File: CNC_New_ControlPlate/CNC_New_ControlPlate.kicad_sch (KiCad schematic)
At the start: 5 parts, among them J1 OTHER, J2 Conn_01x02, J3 STEPPERS, J4 SPINDEL

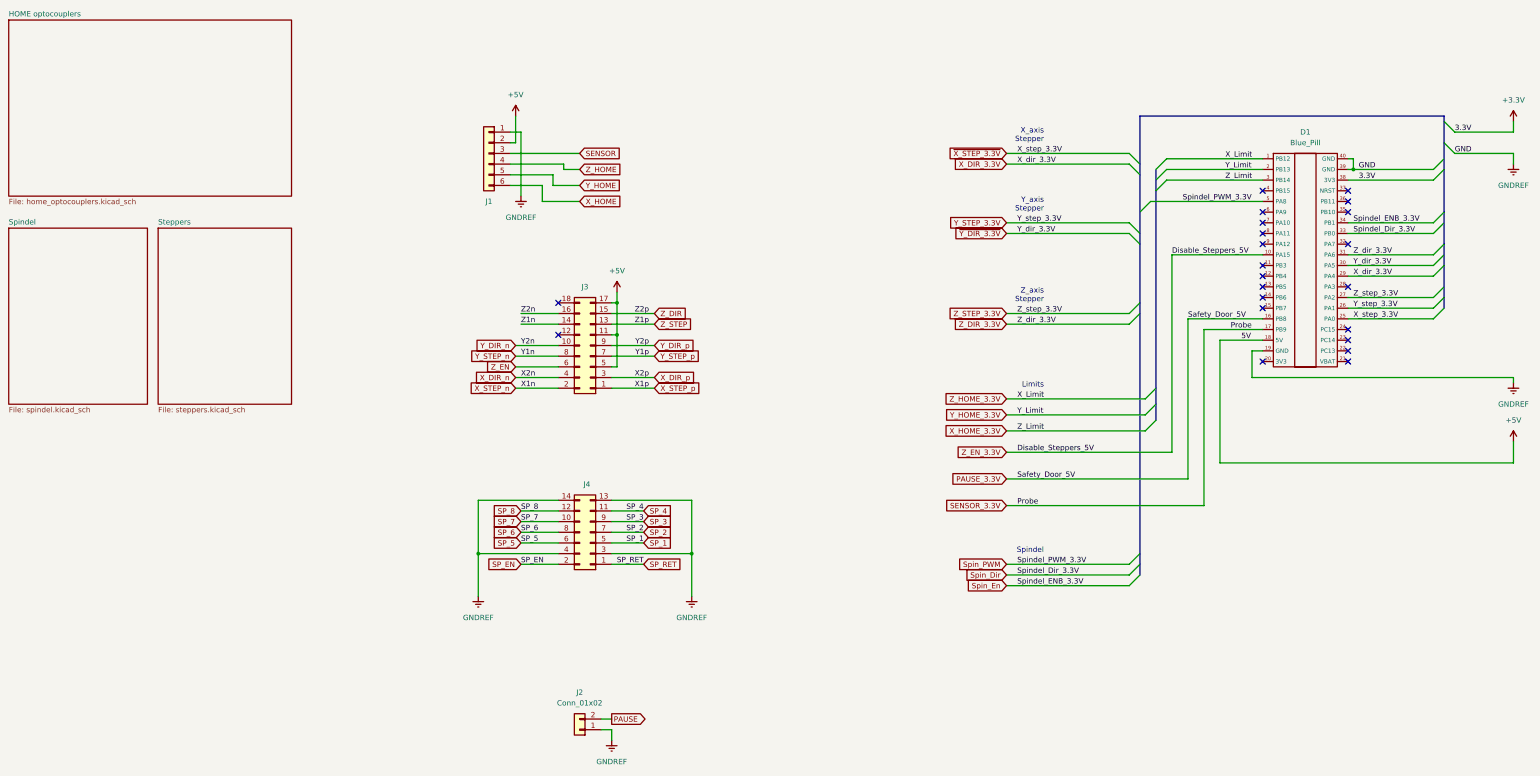
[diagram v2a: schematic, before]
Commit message: Edit footprints
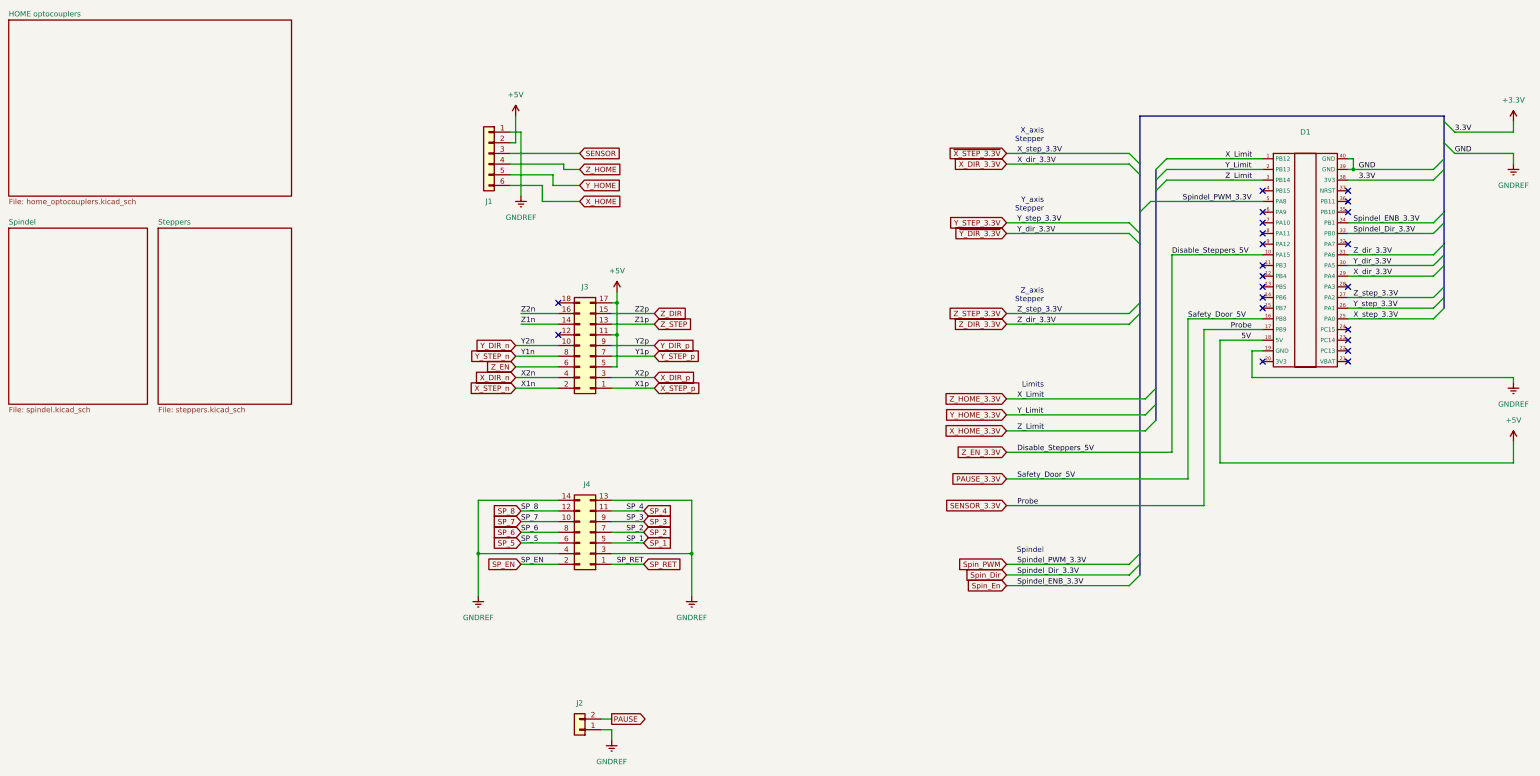
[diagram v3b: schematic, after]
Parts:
- D1: value Blue_Pill -> (none); footprint Module:Maple_Mini -> (none)
- J1: value OTHER -> (none); footprint Connector_JST:JST_XH_B6B-XH-A_1x06_P2.50mm_Vertical -> (none)
- J2: value Conn_01x02 -> (none); footprint Connector_JST:JST_XH_B2B-XH-A_1x02_P2.50mm_Vertical -> (none)
- J3: value STEPPERS -> (none); footprint Connector_PinHeader_2.54mm:PinHeader_2x09_P2.54mm_Vertical -> (none)
- J4: value SPINDEL -> (none); footprint Connector_PinHeader_2.54mm:PinHeader_2x07_P2.54mm_Vertical -> (none)
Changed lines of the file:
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@@
       (effects (font (size 1.27 1.27)) (justify left))
     )
-    (property "Value" "SPINDEL" (id 1) (at 55.8799 132.08 90)
+    (property "Value" "" (id 1) (at 55.8799 132.08 90)
       (effects (font (size 1.27 1.27)) (justify left) hide)
     )
-    (property "Footprint" "Connector_PinHeader_2.54mm:PinHeader_2x07_P2.54mm_Vertical" (id 2) (at 55.88 121.92 0)
+    (property "Footprint" "" (id 2) (at 55.88 121.92 0)
       (effects (font (size 1.27 1.27)) hide)
     )
@@
   )
   (symbol (lib_id "Connector_Generic:Conn_01x02") (at 53.34 168.91 180) (unit 1)
-    (in_bom yes) (on_board yes) (fields_autoplaced)
-    (property "Reference" "J2" (id 0) (at 53.34 160.02 0))
-    (property "Value" "Conn_01x02" (id 1) (at 53.34 162.56 0))
-    (property "Footprint" "Connector_JST:JST_XH_B2B-XH-A_1x02_P2.50mm_Vertical" (id 2) (at 53.34 168.91 0)
+    (in_bom yes) (on_board yes)
+    (property "Reference" "J2" (id 0) (at 53.34 162.56 0))
+    (property "Value" "" (id 1) (at 53.34 162.56 0)
+      (effects (font (size 1.27 1.27)) hide)
+    )
+    (property "Footprint" "" (id 2) (at 53.34 168.91 0)
       (effects (font (size 1.27 1.27)) hide)
     )
@@
     (in_bom yes) (on_board yes)
     (property "Reference" "J1" (id 0) (at 31.75 43.18 0))
-    (property "Value" "OTHER" (id 1) (at 31.75 43.18 0)
-      (effects (font (size 1.27 1.27)) hide)
-    )
-    (property "Footprint" "Connector_JST:JST_XH_B6B-XH-A_1x06_P2.50mm_Vertical" (id 2) (at 31.75 31.75 0)
+    (property "Value" "" (id 1) (at 31.75 43.18 0)
+      (effects (font (size 1.27 1.27)) hide)
+    )
+    (property "Footprint" "" (id 2) (at 31.75 31.75 0)
       (effects (font (size 1.27 1.27)) hide)
     )
@@
     (in_bom yes) (on_board yes) (fields_autoplaced)
     (property "Reference" "D1" (id 0) (at 226.06 26.67 0))
-    (property "Value" "Blue_Pill" (id 1) (at 226.06 29.21 0))
-    (property "Footprint" "Module:Maple_Mini" (id 2) (at 226.06 50.8 0)
+    (property "Value" "" (id 1) (at 226.06 29.21 0))
+    (property "Footprint" "" (id 2) (at 226.06 50.8 0)
       (effects (font (size 1.27 1.27)) hide)
     )
@@
     (in_bom yes) (on_board yes)
     (property "Reference" "J3" (id 0) (at 54.61 63.5 0))
-    (property "Value" "STEPPERS" (id 1) (at 54.61 63.5 0)
-      (effects (font (size 1.27 1.27)) hide)
-    )
-    (property "Footprint" "Connector_PinHeader_2.54mm:PinHeader_2x09_P2.54mm_Vertical" (id 2) (at 55.88 77.47 0)
+    (property "Value" "" (id 1) (at 54.61 63.5 0)
+      (effects (font (size 1.27 1.27)) hide)
+    )
+    (property "Footprint" "" (id 2) (at 55.88 77.47 0)
       (effects (font (size 1.27 1.27)) hide)
     )
@@
     )
     (path "/07e4ffe7-a231-410f-8aa1-cd8347b537a5/95995794-09b8-414e-a750-6d314fcef54c"
-      (reference "D2") (unit 1) (value "D_Zener_1.3V") (footprint "Diode_SMD:D_0603_1608Metric")
-    )
-    (path "/07e4ffe7-a231-410f-8aa1-cd8347b537a5/79cdc865-5b45-4792-9206-5439e8ea1294"
-      (reference "D3") (unit 1) (value "D_Zener_1.3V") (footprint "Diode_SMD:D_0603_1608Metric")
+      (reference "D2") (unit 1) (value "D_Zener_1.3V") (footprint "Diode_THT:D_A-405_P7.62mm_Horizontal")
     )
     (path "/07e4ffe7-a231-410f-8aa1-cd8347b537a5/234c598a-338f-48e2-bbcb-cc75d819923a"
@@
       (reference "D5") (unit 1) (value "D_Zener_1.3V") (footprint "Diode_SMD:D_0603_1608Metric")
     )
-    (path "/07e4ffe7-a231-410f-8aa1-cd8347b537a5/a8d57daf-e188-43f3-9de0-b9baef702578"
-      (reference "D6") (unit 1) (value "D_Zener_1.3V") (footprint "Diode_SMD:D_0603_1608Metric")
-    )
     (path "/cddb5583-7ddf-474c-aeca-fbc0e04243fc/813a06e9-1786-45a4-97ce-b311e1e20896"
       (reference "D7") (unit 1) (value "SN75ALS192N") (footprint "Package_DIP:DIP-16_W7.62mm_Socket")
     )
-    (path "/07e4ffe7-a231-410f-8aa1-cd8347b537a5/e2099293-451c-44e4-a9f8-cf4488cdfcfc"
-      (reference "FB1") (unit 1) (value "FerriteBead") (footprint "Resistor_SMD:R_0603_1608Metric")
-    )
-    (path "/07e4ffe7-a231-410f-8aa1-cd8347b537a5/f8ffdbf9-0674-41ec-af69-a8c71090d156"
-      (reference "FB2") (unit 1) (value "FerriteBead") (footprint "Resistor_SMD:R_0603_1608Metric")
-    )
-    (path "/07e4ffe7-a231-410f-8aa1-cd8347b537a5/da2675cc-ada3-4c0b-9c03-9334c1009a8c"
-      (reference "FB3") (unit 1) (value "FerriteBead") (footprint "Resistor_SMD:R_0603_1608Metric")
-    )
-    (path "/07e4ffe7-a231-410f-8aa1-cd8347b537a5/9c5bd5d2-ecdb-4048-b835-b5ee55546689"
-      (reference "FB4") (unit 1) (value "FerriteBead") (footprint "Resistor_SMD:R_0603_1608Metric")
+    (path "/07e4ffe7-a231-410f-8aa1-cd8347b537a5/66477fc1-579a-4ecd-8ae5-e302aa74469d"
+      (reference "D?") (unit 1) (value "D_Zener_1.3V") (footprint "Diode_THT:D_A-405_P7.62mm_Horizontal")
+    )
+    (path "/07e4ffe7-a231-410f-8aa1-cd8347b537a5/917c91b2-cda4-4d54-a511-11fe02061654"
+      (reference "D?") (unit 1) (value "D_Zener_1.3V") (footprint "Diode_THT:D_A-405_P7.62mm_Horizontal")
+    )
+    (path "/07e4ffe7-a231-410f-8aa1-cd8347b537a5/98c12070-eb89-468e-84b1-06986c8d4a2b"
+      (reference "D?") (unit 1) (value "D_Zener_1.3V") (footprint "Diode_THT:D_A-405_P7.62mm_Horizontal")
+    )
+    (path "/07e4ffe7-a231-410f-8aa1-cd8347b537a5/fe13ba6c-779e-4d09-93d5-8c6912df6cfe"
+      (reference "D?") (unit 1) (value "D_Zener_1.3V") (footprint "Diode_THT:D_A-405_P7.62mm_Horizontal")
     )
     (path "/07e4ffe7-a231-410f-8aa1-cd8347b537a5/90ff4918-d642-483f-9793-ab40184cace1"
-      (reference "FB5") (unit 1) (value "FerriteBead") (footprint "Resistor_SMD:R_0603_1608Metric")
+      (reference "FB5") (unit 1) (value "FerriteBead") (footprint "Resistor_THT:R_Axial_DIN0207_L6.3mm_D2.5mm_P7.62mm_Horizontal")
+    )
+    (path "/07e4ffe7-a231-410f-8aa1-cd8347b537a5/0021bff5-f1cb-4cf9-8522-7c2be30a9d3d"
+      (reference "FB?") (unit 1) (value "FerriteBead") (footprint "Resistor_THT:R_Axial_DIN0207_L6.3mm_D2.5mm_P7.62mm_Horizontal")
+    )
+    (path "/07e4ffe7-a231-410f-8aa1-cd8347b537a5/040d831f-1c86-4ce9-8bdf-bbf55f83e8d3"
+      (reference "FB?") (unit 1) (value "FerriteBead") (footprint "Resistor_THT:R_Axial_DIN0207_L6.3mm_D2.5mm_P7.62mm_Horizontal")
+    )
+    (path "/07e4ffe7-a231-410f-8aa1-cd8347b537a5/39a10fc8-631b-4d65-a8b5-e458bc57a7ce"
+      (reference "FB?") (unit 1) (value "FerriteBead") (footprint "Resistor_THT:R_Axial_DIN0207_L6.3mm_D2.5mm_P7.62mm_Horizontal")
+    )
+    (path "/07e4ffe7-a231-410f-8aa1-cd8347b537a5/cae5d306-31a5-4d4b-a8a2-c1cff0d0ac20"
+      (reference "FB?") (unit 1) (value "FerriteBead") (footprint "Resistor_THT:R_Axial_DIN0207_L6.3mm_D2.5mm_P7.62mm_Horizontal")
     )
     (path "/bed6146f-bd23-4c63-989f-3dd1365a106a"
@@
       (reference "R3") (unit 1) (value "200") (footprint "Resistor_SMD:R_0603_1608Metric")
     )
-    (path "/07e4ffe7-a231-410f-8aa1-cd8347b537a5/86f8d295-2bf8-46bf-bf65-f98ff1b93f57"
-      (reference "R4") (unit 1) (value "200") (footprint "Resistor_SMD:R_0603_1608Metric")
-    )
-    (path "/07e4ffe7-a231-410f-8aa1-cd8347b537a5/141adfea-00ae-462f-bbc2-a5f33915316e"
-      (reference "R5") (unit 1) (value "200") (footprint "Resistor_SMD:R_0603_1608Metric")
-    )
     (path "/07e4ffe7-a231-410f-8aa1-cd8347b537a5/aaeef9b1-d86f-439d-8ab2-8a4e6169e78f"

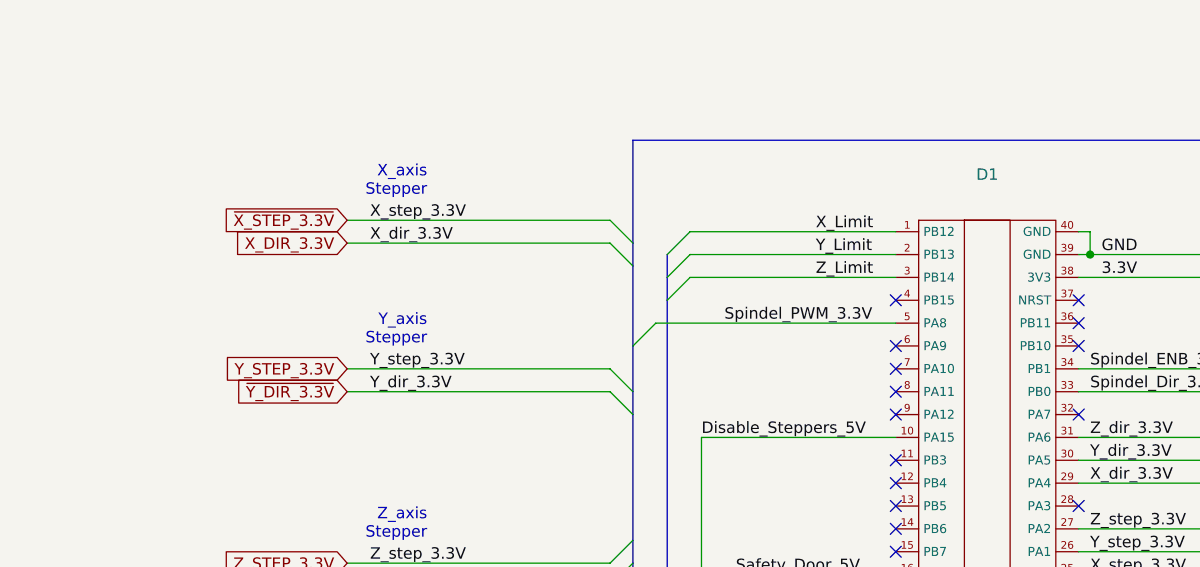
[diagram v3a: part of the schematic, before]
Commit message: [*] Разводка платы в один слой (осталось 7 перемычек)
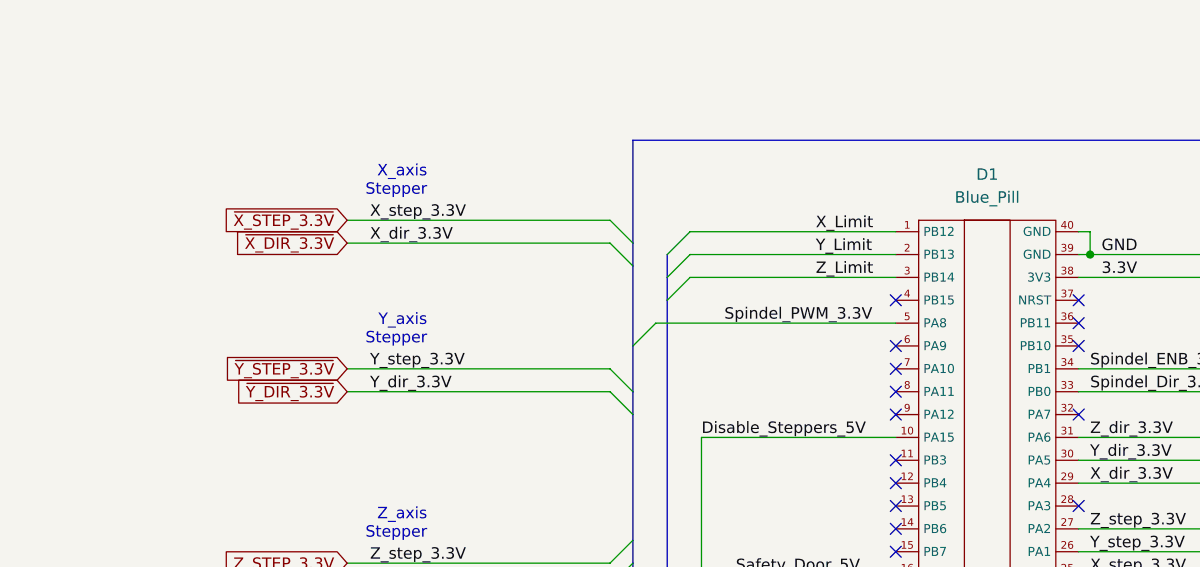
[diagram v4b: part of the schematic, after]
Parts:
- D1: value (none) -> Blue_Pill; footprint (none) -> Module:Maple_Mini
- J1: value (none) -> OTHER; footprint (none) -> Connector_JST:JST_XH_B6B-XH-A_1x06_P2.50mm_Vertical
- J2: value (none) -> Conn_01x02; footprint (none) -> Connector_JST:JST_XH_B2B-XH-A_1x02_P2.50mm_Vertical
- J3: value (none) -> STEPPERS; footprint (none) -> Connector_PinHeader_2.54mm:PinHeader_2x09_P2.54mm_Vertical
- J4: value (none) -> SPINDEL; footprint (none) -> Connector_PinHeader_2.54mm:PinHeader_2x07_P2.54mm_Vertical
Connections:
- net X_DIR_3.3V renamed ~{X_DIR_3.3V}
- net Y_STEP_3.3V renamed ~{Y_STEP_3.3V}

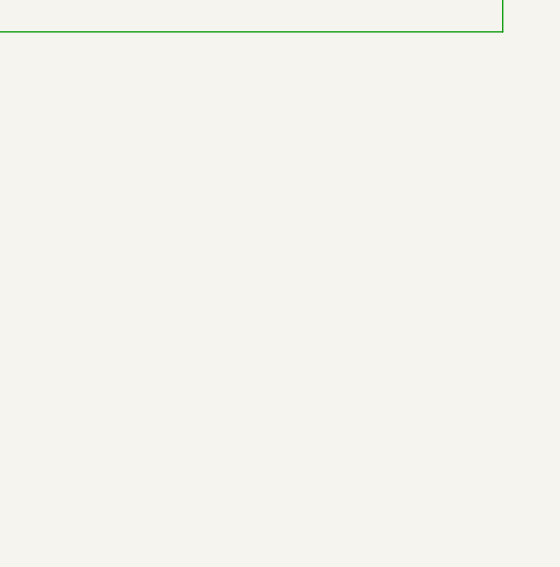
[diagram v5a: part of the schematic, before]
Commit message: [+] Добавлен разъем питания
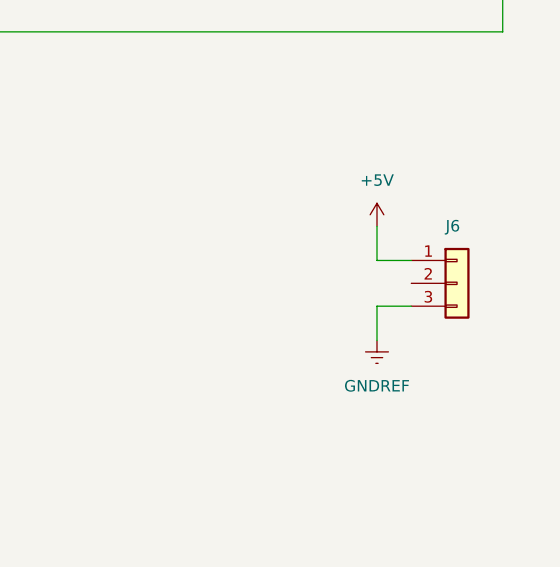
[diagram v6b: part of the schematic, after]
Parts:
- added J6: Conn_01x03, Connector_JST:JST_VH_B3P-VH_1x03_P3.96mm_Vertical, symbol Connector_Generic:Conn_01x03
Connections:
- net +5V: now also J6.1 (Pin_1)
- net GNDREF: now also J6.3 (Pin_3)
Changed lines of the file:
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@@
+    (stroke (width 0) (type default) (color 0 0 0 0))
+  )
+  (wire (pts (xy 261.62 127) (xy 261.62 130.81))
     (stroke (width 0) (type default) (color 0 0 0 0))
   )
@@
     (stroke (width 0) (type default) (color 0 0 0 0))
   )
+  (wire (pts (xy 261.62 139.7) (xy 261.62 135.89))
+    (stroke (width 0) (type default) (color 0 0 0 0))
+  )
   (wire (pts (xy 62.23 64.77) (xy 62.23 67.31))
     (stroke (width 0) (type default) (color 0 0 0 0))
@@
     (stroke (width 0) (type default) (color 0 0 0 0))
   )
+  (wire (pts (xy 261.62 135.89) (xy 265.43 135.89))
+    (stroke (width 0) (type default) (color 0 0 0 0))
+  )
   (wire (pts (xy 236.22 68.58) (xy 256.54 68.58))
     (stroke (width 0) (type default) (color 0 0 0 0))
@@
   )
   (bus (pts (xy 190.5 35.56) (xy 190.5 38.1))
+    (stroke (width 0) (type default) (color 0 0 0 0))
+  )
+  (wire (pts (xy 265.43 130.81) (xy 261.62 130.81))
     (stroke (width 0) (type default) (color 0 0 0 0))
   )
@@
     (pin "9")
   )
+  (symbol (lib_id "power:GNDREF") (at 261.62 139.7 0) (unit 1)
+    (in_bom yes) (on_board yes) (fields_autoplaced)
+    (property "Reference" "#PWR0102" (id 0) (at 261.62 146.05 0)
+      (effects (font (size 1.27 1.27)) hide)
+    )
+    (property "Value" "GNDREF" (id 1) (at 261.62 144.78 0))
+    (property "Footprint" "" (id 2) (at 261.62 139.7 0)
+      (effects (font (size 1.27 1.27)) hide)
+    )
+    (property "Datasheet" "" (id 3) (at 261.62 139.7 0)
+      (effects (font (size 1.27 1.27)) hide)
+    )
+    (pin "1")
+  )
   (symbol (lib_id "power:GNDREF") (at 29.21 137.16 0) (mirror y) (unit 1)
     (in_bom yes) (on_board yes) (fields_autoplaced)
@@
     )
     (property "Datasheet" "" (id 3) (at 29.21 137.16 0)
+      (effects (font (size 1.27 1.27)) hide)
+    )
+    (pin "1")
+  )
+  (symbol (lib_id "power:+5V") (at 261.62 127 0) (unit 1)
+    (in_bom yes) (on_board yes) (fields_autoplaced)
+    (property "Reference" "#PWR0101" (id 0) (at 261.62 130.81 0)
+      (effects (font (size 1.27 1.27)) hide)
+    )
+    (property "Value" "+5V" (id 1) (at 261.62 121.92 0))
+    (property "Footprint" "" (id 2) (at 261.62 127 0)
+      (effects (font (size 1.27 1.27)) hide)
+    )
+    (property "Datasheet" "" (id 3) (at 261.62 127 0)
       (effects (font (size 1.27 1.27)) hide)
     )
@@
     )
     (pin "1")
+  )
+  (symbol (lib_id "Connector_Generic:Conn_01x03") (at 270.51 133.35 0) (unit 1)
+    (in_bom yes) (on_board yes)
+    (property "Reference" "J6" (id 0) (at 269.24 127 0)
+      (effects (font (size 1.27 1.27)) (justify left))
+    )
+    (property "Value" "Conn_01x03" (id 1) (at 273.05 134.6199 0)
+      (effects (font (size 1.27 1.27)) (justify left) hide)
+    )
+    (property "Footprint" "Connector_JST:JST_VH_B3P-VH_1x03_P3.96mm_Vertical" (id 2) (at 270.51 133.35 0)
+      (effects (font (size 1.27 1.27)) hide)
+    )
+    (property "Datasheet" "~" (id 3) (at 270.51 133.35 0)
+      (effects (font (size 1.27 1.27)) hide)
+    )
+    (pin "1")
+    (pin "2")
+    (pin "3")
   )
   (symbol (lib_id "power:GNDREF") (at 80.01 137.16 0) (unit 1)
@@
       (reference "#PWR050") (unit 1) (value "GNDREF") (footprint "")
     )
+    (path "/3ae16155-74e2-4f11-b5c5-b45179358803"
+      (reference "#PWR0101") (unit 1) (value "+5V") (footprint "")
+    )
+    (path "/1d3f1a83-1e1c-48e1-97d2-dbba7694401e"
+      (reference "#PWR0102") (unit 1) (value "GNDREF") (footprint "")
+    )
     (path "/cddb5583-7ddf-474c-aeca-fbc0e04243fc/bee94e64-9b9e-4b4f-8b10-3ab0d343f888"
       (reference "C1") (unit 1) (value "100 nF") (footprint "Capacitor_SMD:C_0603_1608Metric_Pad1.08x0.95mm_HandSolder")
@@
       (reference "J4") (unit 1) (value "SPINDEL") (footprint "Connector_PinHeader_2.54mm:PinHeader_2x07_P2.54mm_Vertical")
     )
+    (path "/b1a35037-868f-4bee-93c8-0efe0a577fa7"
+      (reference "J6") (unit 1) (value "Conn_01x03") (footprint "Connector_JST:JST_VH_B3P-VH_1x03_P3.96mm_Vertical")
+    )
     (path "/07e4ffe7-a231-410f-8aa1-cd8347b537a5/8c9aa3a4-c2cf-4c05-9701-54980603a114"
